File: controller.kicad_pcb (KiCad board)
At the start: 2 copper layers, 62.5 x 50.2 mm, 44 parts, among them J1 Barrel_Jack_MountingPin, J2 Conn_01x02_Pin, J3 Conn_01x07_Pin, J4 Screw_Terminal_01x06, J5 Conn_01x03_Pin, Q1 IRLTS6342TRPBF, Q2 IRLTS6342TRPBF, Q3 IRLTS6342TRPBF, Q4 IRLTS6342TRPBF, Q5 IRLTS6342TRPBF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

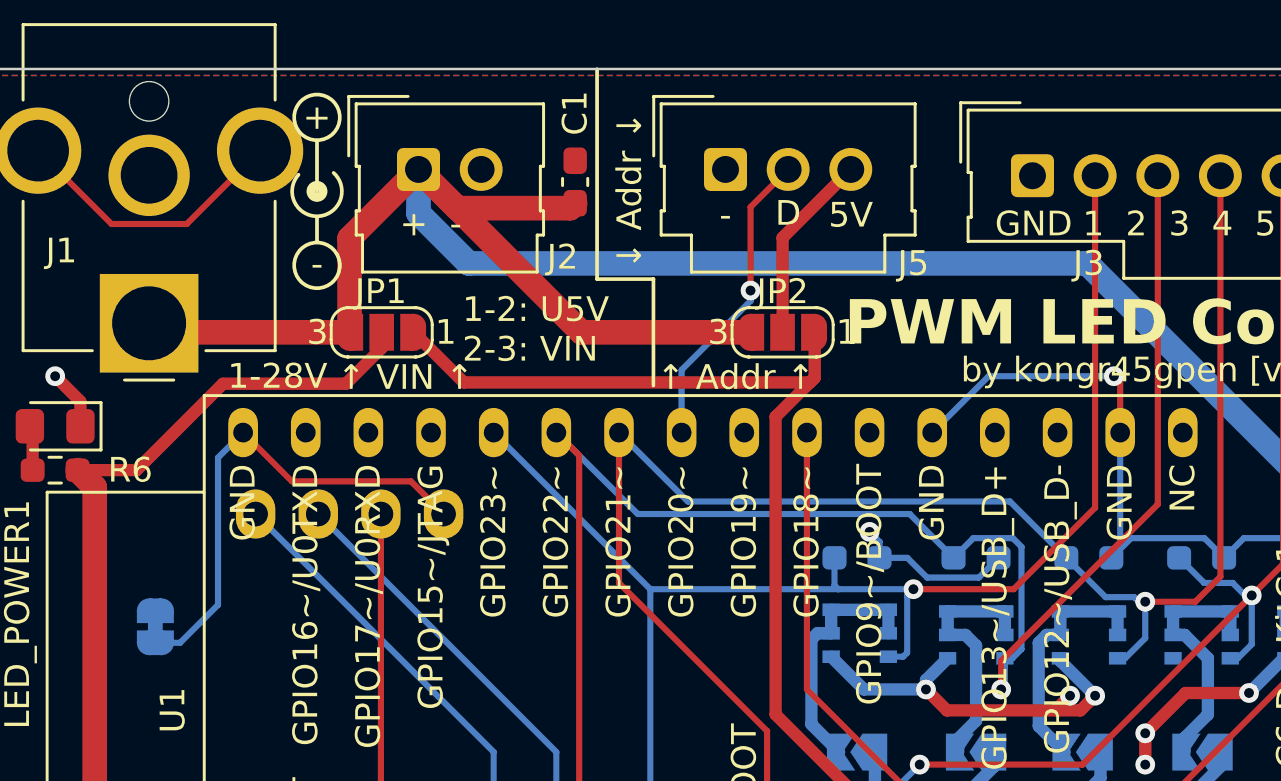
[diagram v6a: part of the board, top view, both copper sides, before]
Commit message: Add teardrops and beautify some traces
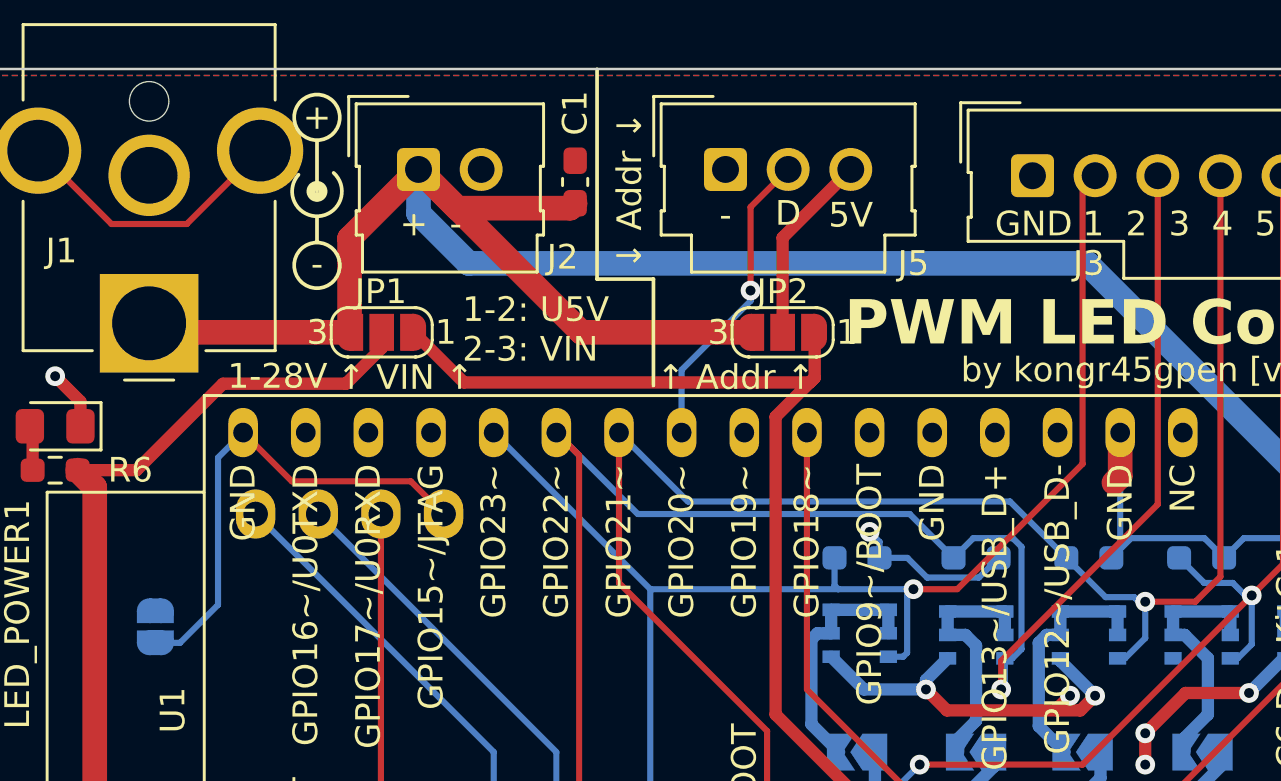
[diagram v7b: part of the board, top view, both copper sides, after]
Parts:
- JP3: footprint Jumper:SolderJumper-2_P1.3mm_Bridged_RoundedPad1.0x1.5mm -> Jumper:SolderJumper-2_P1.3mm_Open_RoundedPad1.0x1.5mm
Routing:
- net GND: track 85.7 -> 77.2 mm, vias 7 -> 6
- net /PWM1: track 72.9 -> 71.6 mm
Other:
- board text added: "Solder me!"
